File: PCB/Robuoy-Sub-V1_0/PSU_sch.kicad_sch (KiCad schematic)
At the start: 23 parts, among them U7 TLV61046ADB, U8 TLV61046ADB

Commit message: Sub pcb started
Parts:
- added C1: 10nF, symbol Device:C_Small
- added D1: B340A, Diode_SMD:D_SMA, symbol Device:D_Schottky
- added L3: 33uH/2A, symbol Device:L_Small
- added U1: TPS5430DDAR, Package_SO:HTSOP-8-1EP_3.9x4.9mm_P1.27mm_EP2.4x3.2mm_ThermalVias, symbol NicE:TPS5430DDAR
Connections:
- new net: C1.1, D1.1 (K), L3.1, U1.8 (PH)
- new net: C1.2, U1.1 (BOOT)

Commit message: Schematic changes not yet finished!
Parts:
- removed C4: 4.7uF, symbol Device:C_Small
- removed C7: 100nF, symbol Device:C_Small
- removed L2: 10uH, symbol Device:L_Small
- removed R10, R9: 15K, symbol Device:R_Small
- removed R11: 51K, symbol Device:R_Small
- removed R12: 16K, symbol Device:R_Small
- removed TP5: 0.795V, symbol Connector:TestPoint_Small
- removed TP9: 3V3, symbol Connector:TestPoint_Small
- removed U8: TLV61046ADB, Package_TO_SOT_SMD:SOT-23-6, symbol Regulator_Switching:TLV61046ADB
- added C201, C203: 100u/16V, Capacitor_SMD:C_1210_3225Metric, symbol Device:C_Small
- added C202: 220u/50V, A_Device:CP_ALU_D10x10.5, symbol Device:C_Polarized_Small
- added C204, C206, C207: 100n, A_Device:C_0603, symbol Device:C_Small
- added C205: 100nF, symbol Device:C_Small
- added D201: SM4007PL, A_Device:D_SOD-123_2.85x1.8x1.3, symbol Device:D_Small
- added J201: ESCBB, symbol Connector:Conn_01x02_Socket
- added J202: ESCSB, symbol Connector:Conn_01x02_Socket
- added J203: Accu, A_Connector:AMASS_XT60-M_1x02_P7.20mm_Vertical, symbol Connector:Conn_01x02_Socket
- added J204: PWR_Charger, A_Connector:AMASS_XT60-M_1x02_P7.20mm_Vertical, symbol Connector:Conn_01x02_Socket
- added J205: LoadbalanceAccu1, symbol Connector:Conn_01x07_Pin
- added J206: LoadbalanceAccu2, symbol Connector:Conn_01x07_Pin
- added J207: LoadbalanceCharger, symbol Connector:Conn_01x07_Socket
- added J208: Conn_01x10, symbol Connector_Generic:Conn_01x10
- added Q201, Q203: SUD19P06-60-GE3, Package_TO_SOT_SMD:TO-252-2, symbol Transistor_FET:SUD19P06-60
- added Q202, Q204: MMBT3904, Package_TO_SOT_SMD:SOT-23, symbol Transistor_BJT:MMBT3904
- added R201, R205, R207: 18K, symbol Device:R_Small
- added R204, R206, R208: 10K, symbol Device:R_Small
- added R209, R210, R211, R213: 1k, A_Device:R_0603, symbol Device:R_Small
- added R212: 6.2k, A_Device:R_0603, symbol Device:R_Small
- added SW201: SS-12D11-G050/On-Off, symbol Switch:SW_DPST_x2
- added TP202: Vcell, A_Pads_Pins:Testpoint_0.6x1.0, symbol Connector:TestPoint_Flag
- C3: value 4.7uF -> 4.7uF`/10V
- R19: value 1.5k -> 1.8k; LCSC C22843 -> (none)
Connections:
- net Enable is gone; now on net +3.3V: U7.4 (EN)
- net VBUS is gone; now on net +3.3V: C6.1, L1.1, U7.6 (VI)
- net +3.3V: now also L3.2, C201.1, C203.1, C204.1, D201.1 (K), R201.1
- net +5V: now also C205.1
- net GND: now also C3.2, C6.2, D1.2 (A), R8.2, U1.6 (GND), U1.9 (PAD), U7.2 (GND), C201.2, C202.2, C203.2, C204.2, C205.2, C206.2, C207.2, J201.1 (Pin_1), J202.1 (Pin_1), J203.1 (Pin_1), J204.1 (Pin_1), J208.9 (Pin_9), Q202.2 (E), Q204.2 (E), R204.2, R211.2, R213.2
- net at U1.4 (Vsens): now also R201.2, R204.1
- net +VSW: now reaches U1.7 (Vin)
- net +VSW: now also C202.1, C206.1, J208.8 (Pin_8), R212.1, SW201.2 (B)
- new net: J201.2 (Pin_2), Q203.2 (D)
- new net: Q204.1 (B), R210.2
- new net: J205.1 (Pin_1), J206.1 (Pin_1), J207.1 (Pin_1), J208.1 (Pin_1)
- new net: J205.2 (Pin_2), J206.2 (Pin_2), J207.2 (Pin_2), J208.2 (Pin_2)
- new net: J205.3 (Pin_3), J206.3 (Pin_3), J207.3 (Pin_3), J208.3 (Pin_3)
- new net: J205.4 (Pin_4), J206.4 (Pin_4), J207.4 (Pin_4), J208.4 (Pin_4)
- new net: J205.5 (Pin_5), J206.5 (Pin_5), J207.5 (Pin_5), J208.5 (Pin_5)
- new net: J205.6 (Pin_6), J206.6 (Pin_6), J207.6 (Pin_6), J208.6 (Pin_6)
- new net: J205.7 (Pin_7), J206.7 (Pin_7), J207.7 (Pin_7), J208.7 (Pin_7)
- new net: Q202.1 (B), R209.2
- new net: Q202.3 (C), R208.2
- new net: J202.2 (Pin_2), Q201.2 (D)
- new net: Q203.1 (G), R205.2, R206.1
- new net: Q204.3 (C), R206.2
- new net: Q201.1 (G), R207.2, R208.1
- new net PWR_ESC_BB: R210.1
- new net PWR_ESC_SB: R209.1
- new net Vbatt: C207.1, D201.2 (A), J203.2 (Pin_2), J204.2 (Pin_2), J208.10 (Pin_10), Q201.3 (S), Q203.3 (S), R205.1, R207.1, R211.1, R212.2, R213.1, SW201.1 (A), TP202.1
- no-connect marks 0 -> 1
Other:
- moved on the sheet: C1, C3, C6, D1, D6, D7, L1, L3, R19, R20, R7, R8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

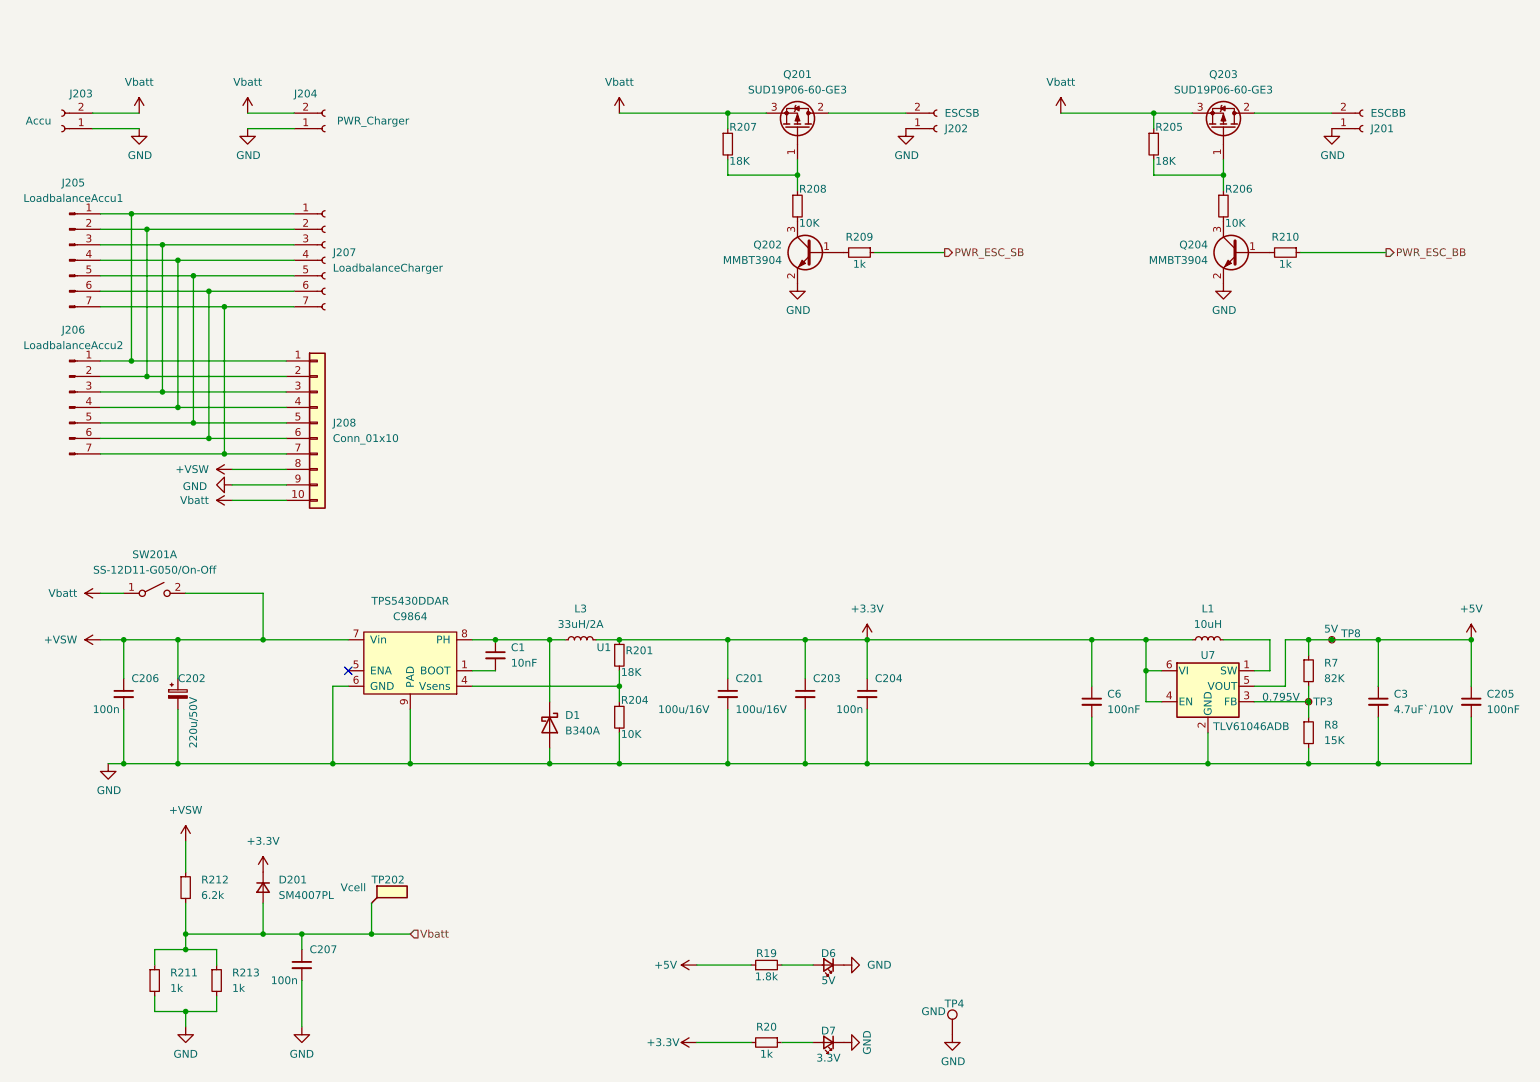
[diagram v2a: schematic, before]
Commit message: Sub ready for routing
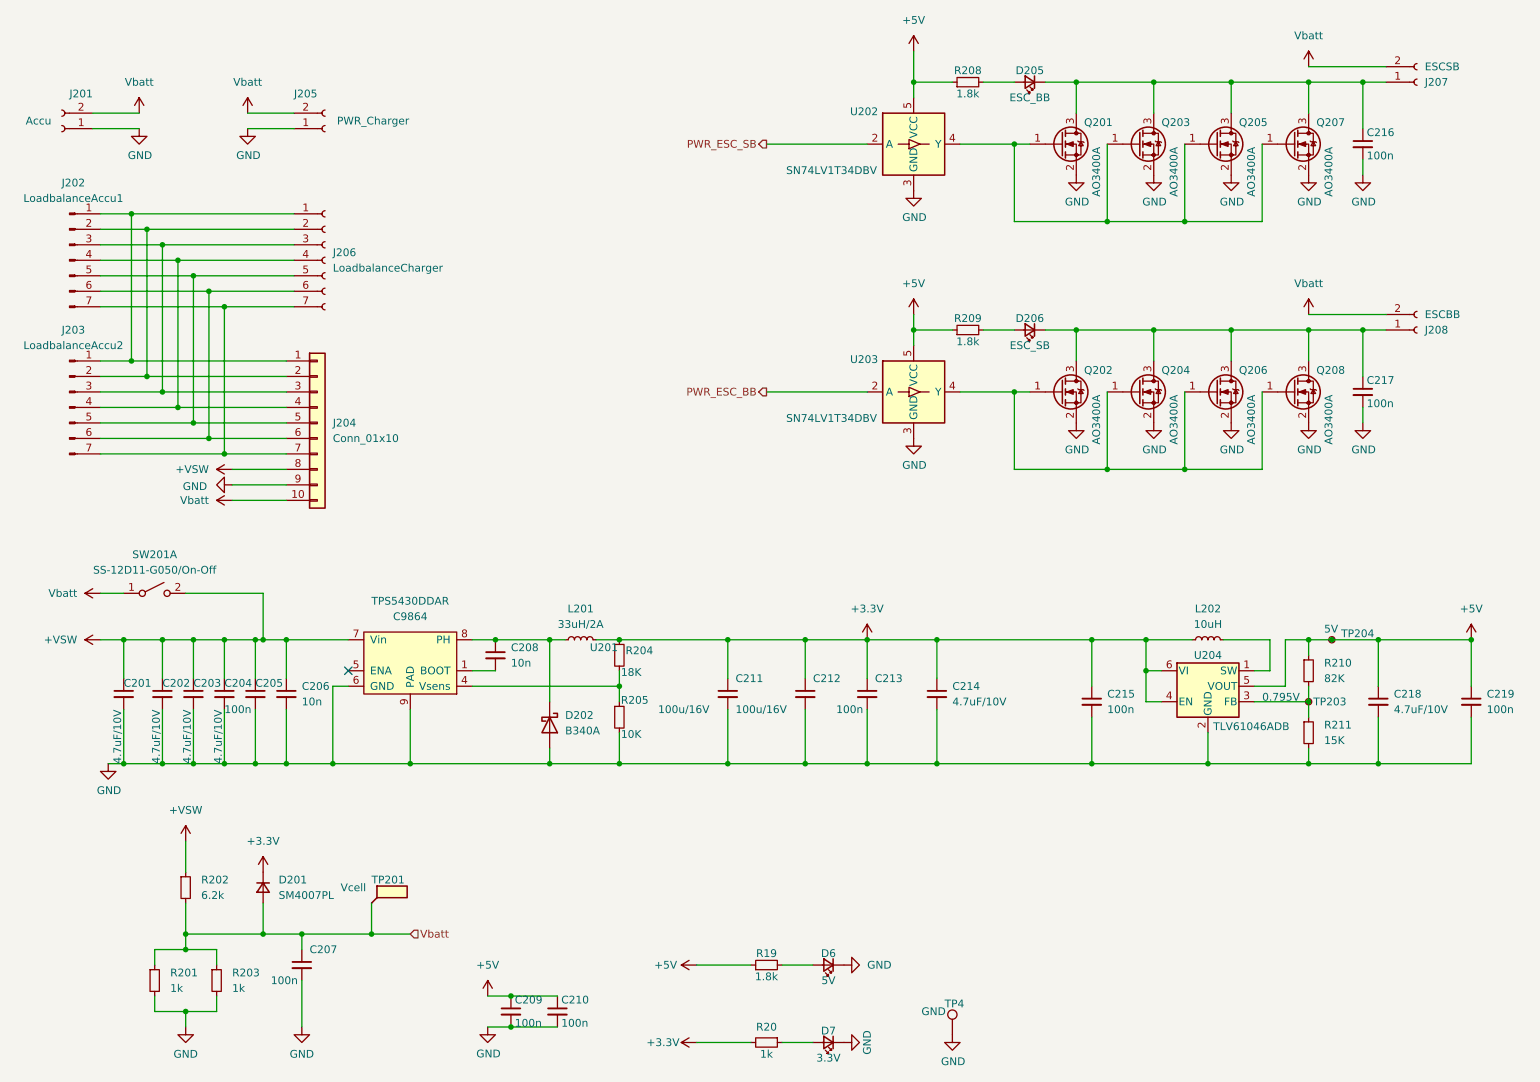
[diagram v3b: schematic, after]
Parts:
- removed C202: 220u/50V, A_Device:CP_ALU_D10x10.5, symbol Device:C_Polarized_Small
- removed Q201, Q203: SUD19P06-60-GE3, Package_TO_SOT_SMD:TO-252-2, symbol Transistor_FET:SUD19P06-60
- removed Q202, Q204: MMBT3904, Package_TO_SOT_SMD:SOT-23, symbol Transistor_BJT:MMBT3904
- removed R205, R207: 18K, symbol Device:R_Small
- removed R206: 10K, symbol Device:R_Small
- removed R210: 1k, A_Device:R_0603, symbol Device:R_Small
- added C201, C202, C203, C204, C214: 4.7uF/10V, A_Device:C_1206_(1.6), symbol Device:C_Small
- added C206: 10n, A_Device:C_0603, symbol Device:C_Small
- added C209, C210, C216, C217: 100n, A_Device:C_0603, symbol Device:C_Small
- added D205: ESC_BB, LED_SMD:LED_0603_1608Metric, symbol Device:LED_Small
- added D206: ESC_SB, LED_SMD:LED_0603_1608Metric, symbol Device:LED_Small
- added Q201, Q202, Q203, Q204, Q205, Q206, Q207, Q208: AO3400A, Package_TO_SOT_SMD:SOT-23, symbol Transistor_FET:2N7002
- added U202, U203: SN74LV1T34DBV, Package_TO_SOT_SMD:SOT-23-5, symbol Logic_LevelTranslator:SN74LV1T34DBV
- C208: renamed from C1; value 10nF -> 10n; footprint (none) -> A_Device:C_0603; LCSC (none) -> C1589
- C215: renamed from C6; value 100nF -> 100n; footprint (none) -> A_Device:C_0603; LCSC (none) -> C14663
- C218: renamed from C3; value 4.7uF`/10V -> 4.7uF/10V; footprint (none) -> A_Device:C_1206_(1.6); LCSC (none) -> C29823
- C219: renamed from C205; value 100nF -> 100n; footprint (none) -> A_Device:C_0603; LCSC (none) -> C14663
- J202: renamed from J205; footprint (none) -> Connector_JST:JST_EH_B7B-EH-A_1x07_P2.50mm_Vertical
- J203: renamed from J206; footprint (none) -> Connector_JST:JST_EH_B7B-EH-A_1x07_P2.50mm_Vertical
- J204: renamed from J208; footprint (none) -> Connector_JST:JST_EH_B10B-EH-A_1x10_P2.50mm_Vertical
- J205: renamed from J204; footprint A_Connector:AMASS_XT60-M_1x02_P7.20mm_Vertical -> A_Connector:AMASS_XT60-F_1x02_P7.20mm_Vertical
- J206: renamed from J207; footprint (none) -> Connector_JST:JST_EH_B7B-EH-A_1x07_P2.50mm_Vertical
- J207: renamed from J202; footprint (none) -> A_Connector:AMASS_XT60-F_1x02_P7.20mm_Vertical
- J208: renamed from J201; footprint (none) -> A_Connector:AMASS_XT60-F_1x02_P7.20mm_Vertical
- L201: renamed from L3; footprint (none) -> A_Device:L_6.6x7.0mm
- L202: renamed from L1; footprint (none) -> A_Device:FTC252012S
- R204: renamed from R201; footprint (none) -> A_Device:R_0603
- R205: renamed from R204; footprint (none) -> A_Device:R_0603
- R208: value 10K -> 1.8k; footprint (none) -> A_Device:R_0603
- R209: value 1k -> 1.8k; LCSC C21190 -> (none)
- R210: renamed from R7; footprint (none) -> A_Device:R_0603
- R211: renamed from R8; footprint (none) -> A_Device:R_0603
- SW201: footprint (none) -> A_Connector:SS-12D10L5; LCSC C17179528 -> C319012
- TP201: renamed from TP202; footprint A_Pads_Pins:Testpoint_0.6x1.0 -> A_Pads_Pins:Testpoint_0.9x1.5
- TP203: renamed from TP3; footprint (none) -> A_Pads_Pins:Testpoint_0.9x1.5
- TP204: renamed from TP8; footprint (none) -> A_Pads_Pins:Testpoint_0.9x1.5
- renumbered C206 to C205, C201 to C211, C203 to C212, C204 to C213, D1 to D202, J203 to J201, R211 to R201, R212 to R202, R213 to R203, U1 to U201, U7 to U204
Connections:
- net +3.3V: now also C214.1
- net +5V: now also R208.1, R209.1, C209.1, C210.1, U202.5 (VCC), U203.5 (VCC)
- net +VSW: now also C201.1, C202.1, C203.1, C204.1, C206.1
- net GND: now also C201.2, C202.2, C203.2, C204.2, C206.2, C209.2, C210.2, C214.2, C216.2, C217.2, Q201.2 (S), Q202.2 (S), Q203.2 (S), Q204.2 (S), Q205.2 (S), Q206.2 (S), Q207.2 (S), Q208.2 (S), U202.3 (GND), U203.3 (GND); no longer J207.1 (Pin_1), J208.1 (Pin_1)
- net PWR_ESC_BB: now also U203.2 (A)
- net PWR_ESC_SB: now also U202.2 (A); no longer R209.1
- net Vbatt: now also J207.2 (Pin_2), J208.2 (Pin_2)
- net at R209.2: now also D206.2 (A)
- net at R208.2: now also D205.2 (A)
- new net: C217.1, D206.1 (K), J208.1 (Pin_1), Q202.3 (D), Q204.3 (D), Q206.3 (D), Q208.3 (D)
- new net: Q202.1 (G), Q204.1 (G), Q206.1 (G), Q208.1 (G), U203.4 (Y)
- new net: Q201.1 (G), Q203.1 (G), Q205.1 (G), Q207.1 (G), U202.4 (Y)
- new net: C216.1, D205.1 (K), J207.1 (Pin_1), Q201.3 (D), Q203.3 (D), Q205.3 (D), Q207.3 (D)
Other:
- moved on the sheet: C205, J207, J208

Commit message: Pcb's getting ready for routing
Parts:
- C206, C208: LCSC C1589 -> C57112
- D205, D206, D6, D7: footprint LED_SMD:LED_0603_1608Metric -> A_Passive:LED_0805; LCSC C72043 -> C2297
- J202, J203, J206: footprint Connector_JST:JST_EH_B7B-EH-A_1x07_P2.50mm_Vertical -> Connector_JST:JST_XH_B7B-XH-A_1x07_P2.50mm_Vertical; LCSC (none) -> C5341206
- J204: footprint Connector_JST:JST_EH_B10B-EH-A_1x10_P2.50mm_Vertical -> Connector_JST:JST_XH_B10B-XH-A_1x10_P2.50mm_Vertical; LCSC (none) -> C7434315
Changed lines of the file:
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@@
 			)
 		)
-		(property "Footprint" "LED_SMD:LED_0603_1608Metric"
+		(property "Footprint" "A_Passive:LED_0805"
 			(at 182.88 73.66 90)
 			(effects
@@
 			)
 		)
-		(property "LCSC" "C72043"
+		(property "LCSC" "C2297"
 			(at 182.88 73.66 0)
 			(effects
@@
 			)
 		)
-		(property "Footprint" "Connector_JST:JST_EH_B7B-EH-A_1x07_P2.50mm_Vertical"
+		(property "Footprint" "Connector_JST:JST_XH_B7B-XH-A_1x07_P2.50mm_Vertical"
 			(at 25.4 86.36 0)
 			(effects
@@
 			)
 		)
+		(property "LCSC" "C5341206"
+			(at 25.4 86.36 0)
+			(effects
+				(font
+					(size 1.27 1.27)
+				)
+				(hide yes)
+			)
+		)
 		(pin "1"
 		)
@@
 			)
 		)
-		(property "LCSC" "C1589"
+		(property "LCSC" "C57112"
 			(at 60.96 133.35 0)
 			(effects
@@
 			)
 		)
-		(property "Footprint" "LED_SMD:LED_0603_1608Metric"
+		(property "Footprint" "A_Passive:LED_0805"
 			(at 149.86 177.8 90)
 			(effects
@@
 			)
 		)
-		(property "LCSC" "C72043"
+		(property "LCSC" "C2297"
 			(at 149.86 177.8 0)
 			(effects
@@
 			)
 		)
-		(property "Footprint" "LED_SMD:LED_0603_1608Metric"
+		(property "Footprint" "A_Passive:LED_0805"
 			(at 182.88 33.02 90)
 			(effects
@@
 			)
 		)
-		(property "LCSC" "C72043"
+		(property "LCSC" "C2297"
 			(at 182.88 33.02 0)
 			(effects
@@
 			)
 		)
-		(property "Footprint" "LED_SMD:LED_0603_1608Metric"
+		(property "Footprint" "A_Passive:LED_0805"
 			(at 149.86 190.5 90)
 			(effects
@@
 			)
 		)
-		(property "LCSC" "C72043"
+		(property "LCSC" "C2297"
 			(at 149.86 190.5 0)
 			(effects
@@
 			)
 		)
-		(property "Footprint" "Connector_JST:JST_EH_B10B-EH-A_1x10_P2.50mm_Vertical"
+		(property "Footprint" "Connector_JST:JST_XH_B10B-XH-A_1x10_P2.50mm_Vertical"
 			(at 66.04 88.9 0)
 			(effects
@@
 			)
 		)
-		(property "Datasheet" "~"
+		(property "Datasheet" "https://wmsc.lcsc.com/wmsc/upload/file/pdf/v2/lcsc/2312302351_HCTL-HC-XH-10A-G-K_C7434315.pdf"
 			(at 66.04 88.9 0)
 			(effects
@@
 			)
 		)
-		(property "JLCS" ""
+		(property "LCSC" "C7434315"
 			(at 66.04 88.9 0)
 			(effects
@@
 			)
 		)
-		(property "Footprint" "Connector_JST:JST_EH_B7B-EH-A_1x07_P2.50mm_Vertical"
+		(property "Footprint" "Connector_JST:JST_XH_B7B-XH-A_1x07_P2.50mm_Vertical"
 			(at 67.31 62.23 0)
 			(effects
@@
 			)
 		)
-		(property "JLCS" ""
+		(property "LCSC" "C5341206"
 			(at 67.31 62.23 0)
 			(effects
@@
 			)
 		)
-		(property "LCSC" "C1589"
+		(property "LCSC" "C57112"
 			(at 95.25 127 0)
 			(effects
@@
 			)
 		)
-		(property "Footprint" "Connector_JST:JST_EH_B7B-EH-A_1x07_P2.50mm_Vertical"
+		(property "Footprint" "Connector_JST:JST_XH_B7B-XH-A_1x07_P2.50mm_Vertical"
 			(at 25.4 62.23 0)
 			(effects
@@
 			)
 		)
-		(property "JLCS" ""
+		(property "LCSC" "C5341206"
 			(at 25.4 62.23 0)
 			(effects

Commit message: PCB changes. Calulation price changed
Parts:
- J207, J208: LCSC (none) -> C98734
- R204: LCSC (none) -> C25810
- R205: LCSC (none) -> C25804
- R208, R209: LCSC (none) -> C4177
- R210: LCSC (none) -> C23254
- R211: LCSC (none) -> C22809
- U204: LCSC (none) -> C464815
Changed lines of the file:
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@@
 			)
 		)
+		(property "LCSC" "C98734"
+			(at 247.65 73.6601 0)
+			(effects
+				(font
+					(size 1.27 1.27)
+				)
+				(hide yes)
+			)
+		)
 		(pin "2"
 		)
@@
 			)
 		)
+		(property "LCSC" "C25804"
+			(at 115.824 134.366 0)
+			(effects
+				(font
+					(size 1.27 1.27)
+				)
+				(hide yes)
+			)
+		)
 		(pin "2"
 		)
@@
 			)
 		)
+		(property "LCSC" "C25810"
+			(at 116.586 126.238 0)
+			(effects
+				(font
+					(size 1.27 1.27)
+				)
+				(hide yes)
+			)
+		)
 		(pin "2"
 		)
@@
 			)
 		)
+		(property "LCSC" "C464815"
+			(at 212.09 127 0)
+			(effects
+				(font
+					(size 1.27 1.27)
+				)
+				(hide yes)
+			)
+		)
 		(pin "4"
 		)
@@
 			)
 		)
-		(property "JLCS" ""
-			(at 149.86 177.8 0)
-			(effects
-				(font
-					(size 1.27 1.27)
-				)
-				(hide yes)
-			)
-		)
 		(pin "1"
 		)
@@
 			)
 		)
-		(property "LCSC" ""
+		(property "LCSC" "C4177"
 			(at 172.72 33.02 0)
 			(effects
@@
 			)
 		)
+		(property "LCSC" "C23254"
+			(at 231.14 128.2699 0)
+			(effects
+				(font
+					(size 1.27 1.27)
+				)
+				(hide yes)
+			)
+		)
 		(pin "2"
 		)
@@
 			)
 		)
-		(property "JLCS" ""
-			(at 149.86 190.5 0)
-			(effects
-				(font
-					(size 1.27 1.27)
-				)
-				(hide yes)
-			)
-		)
 		(pin "1"
 		)
@@
 			)
 		)
+		(property "LCSC" "C98734"
+			(at 247.65 33.0201 0)
+			(effects
+				(font
+					(size 1.27 1.27)
+				)
+				(hide yes)
+			)
+		)
 		(pin "2"
 		)
@@
 			)
 		)
+		(property "LCSC" "C22809"
+			(at 231.14 138.4299 0)
+			(effects
+				(font
+					(size 1.27 1.27)
+				)
+				(hide yes)
+			)
+		)
 		(pin "2"
 		)
@@
 			)
 		)
-		(property "LCSC" ""
+		(property "LCSC" "C4177"
 			(at 172.72 73.66 0)
 			(effects

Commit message: Sub PCB parts okay
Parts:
- removed J204: Conn_01x10, Connector_JST:JST_XH_B10B-XH-A_1x10_P2.50mm_Vertical, symbol Connector_Generic:Conn_01x10
- removed TP4: GND, A_Pads_Pins:Testpoint_0.9x1.5, symbol Connector:TestPoint
- added J204: CHARGE/ON-OFF, A_Connector:T4140012121000, symbol Connector:Conn_01x12_Socket
- added TP202, TP203: GND, TestPoint:TestPoint_Loop_D2.54mm_Drill1.5mm_Beaded, symbol Connector:TestPoint
- added TP206: 1.221V, A_Pads_Pins:Testpad_2, symbol Connector:TestPoint_Small
- added TP207: ESC_BB-POWER, A_Pads_Pins:Testpad_2, symbol Connector:TestPoint_Small
- added TP208: ESC_SB-POWER, A_Pads_Pins:Testpad_2, symbol Connector:TestPoint_Small
- added TP209: ESC_BB-POWER-5V, A_Pads_Pins:Testpad_2, symbol Connector:TestPoint_Small
- added TP210: ESC_SB-POWER-5V, A_Pads_Pins:Testpad_2, symbol Connector:TestPoint_Small
- TP201: footprint A_Pads_Pins:Testpoint_0.9x1.5 -> A_Pads_Pins:Testpad_2; now left out of the parts list
- TP204: renamed from TP203; footprint A_Pads_Pins:Testpoint_0.9x1.5 -> A_Pads_Pins:Testpad_2; now left out of the parts list
- TP205: renamed from TP204; footprint A_Pads_Pins:Testpoint_0.9x1.5 -> A_Pads_Pins:Testpad_2; now left out of the parts list
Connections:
- net +VSW: now also J204.8 (Pin_8)
- net GND: now also J204.10 (Pin_10), J204.9 (Pin_9), TP202.1, TP203.1
- net PWR_ESC_BB: now also TP207.1
- net PWR_ESC_SB: now also TP208.1
- net Vbatt: now also J204.11 (Pin_11), J204.12 (Pin_12)
- net at Q202.1 (G), Q204.1 (G), Q206.1 (G)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: now also TP209.1
- net at R204.2, R205.1, U201.4 (Vsens): now also TP206.1
- net at Q201.1 (G), Q203.1 (G), Q205.1 (G)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: now also TP210.1
- net at J202.1 (Pin_1), J203.1 (Pin_1), J206.1 (Pin_1): now also J204.1 (Pin_1)
- net at J202.2 (Pin_2), J203.2 (Pin_2), J206.2 (Pin_2): now also J204.2 (Pin_2)
- net at J202.3 (Pin_3), J203.3 (Pin_3), J206.3 (Pin_3): now also J204.3 (Pin_3)
- net at J202.4 (Pin_4), J203.4 (Pin_4), J206.4 (Pin_4): now also J204.4 (Pin_4)
- net at J202.5 (Pin_5), J203.5 (Pin_5), J206.5 (Pin_5): now also J204.5 (Pin_5)
- net at J202.6 (Pin_6), J203.6 (Pin_6), J206.6 (Pin_6): now also J204.6 (Pin_6)
- net at J202.7 (Pin_7), J203.7 (Pin_7), J206.7 (Pin_7): now also J204.7 (Pin_7)
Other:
- moved on the sheet: D6, D7, R19, R20
